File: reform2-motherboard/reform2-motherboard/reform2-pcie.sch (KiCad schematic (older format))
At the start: 31 parts, among them J10 1-2199230-6, J11 48099-5701, U11 679105700

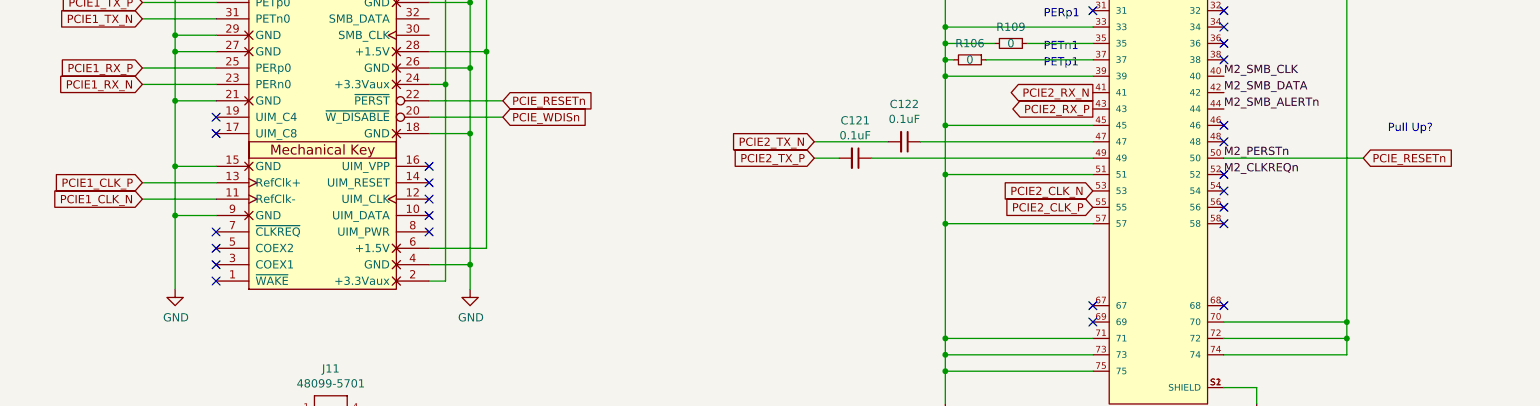
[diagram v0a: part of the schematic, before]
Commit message: WIP: reform 2 motherboard: tweaks for CL-SOM
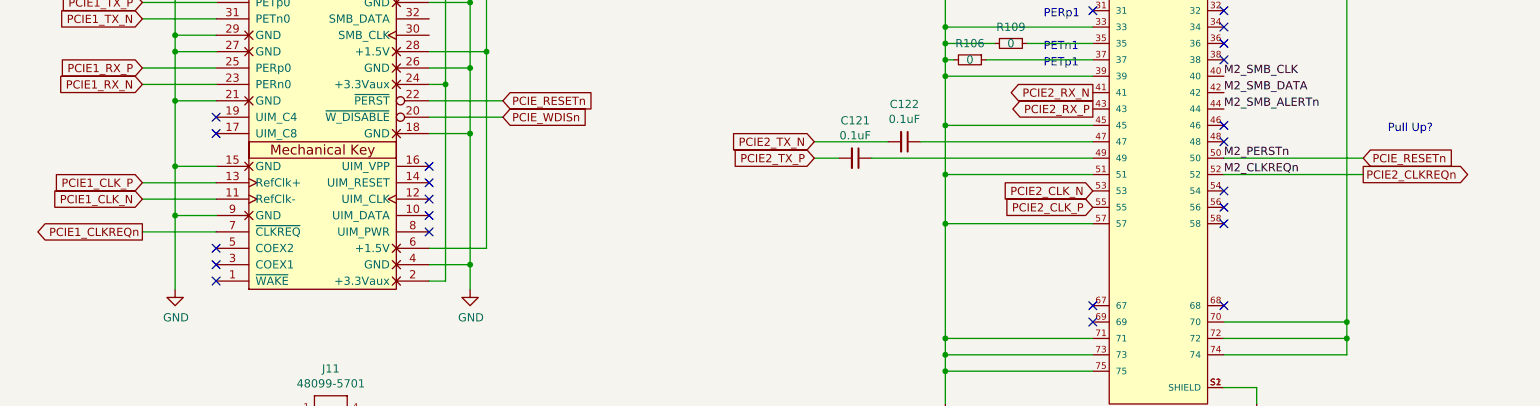
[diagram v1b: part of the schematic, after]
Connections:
- net labels added: PCIE1_CLKREQn, PCIE2_CLKREQn
- wire segments 175 -> 177
- no-connect marks 42 -> 40
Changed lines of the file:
@@
 Sheet 6 9
 Title "MNT Reform 2 PCIe"
-Date "2019-07-03"
-Rev "0.1"
+Date "2019-07-09"
+Rev "0.1.1"
 Comp "MNT Research GmbH"
 Comment1 "https://mntre.com"
@@
 NoConn ~ 2850 4500
 NoConn ~ 2850 4600
-NoConn ~ 2850 5200
 NoConn ~ 2850 5300
 NoConn ~ 2850 5400
@@
 NoConn ~ 4150 4900
 NoConn ~ 4150 4800
-NoConn ~ 9000 4850
 Text GLabel 4600 4500 2    50   Input ~ 0
 PCIE_WDISn
@@
 Wire Wire Line
 	4500 4100 4500 5300
+Text GLabel 2400 5200 0    50   Output ~ 0
+PCIE1_CLKREQn
+Wire Wire Line
+	2850 5200 2400 5200
+Text GLabel 9850 4850 2    50   Output ~ 0
+PCIE2_CLKREQn
+Wire Wire Line
+	9850 4850 9000 4850
 $EndSCHEMATC

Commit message: WIP: reform 2 motherboard: initial power section placement, routing tests
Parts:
- removed C56, C57, C62, C63: 220uF, Capacitor_SMD:CP_Elec_8x10, symbol Device:CP1_Small
- added C123, C124, C126, C83: 47uF, Capacitor_SMD:C_0603_1608Metric, symbol Device:C_Small
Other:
- note added: "TODO: symbol/connector pin mismatch"
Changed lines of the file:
@@
 Sheet 6 9
 Title "MNT Reform 2 PCIe"
-Date "2019-07-09"
-Rev "0.1.1"
+Date "2019-07-10"
+Rev "0.1.2"
 Comp "MNT Research GmbH"
 Comment1 "https://mntre.com"
@@
 	1    0    0    -1
 $EndComp
-$Comp
-L Device:CP1_Small C56
-U 1 1 60FCBB5A
-P 3600 2050
-F 0 "C56" H 3691 2096 50  0000 L CNN
-F 1 "220uF" H 3691 2005 50  0000 L CNN
-F 2 "Capacitor_SMD:CP_Elec_8x10" H 3600 2050 50  0001 C CNN
-F 3 "~" H 3600 2050 50  0001 C CNN
-F 4 "Panasonic" H 3600 2050 50  0001 C CNN "Manufacturer"
-F 5 "EEE-FT1H221GP" H 3600 2050 50  0001 C CNN "Manufacturer_No"
-	1    3600 2050
-	1    0    0    -1
-$EndComp
-$Comp
-L Device:CP1_Small C57
-U 1 1 60FCC62A
-P 4000 2050
-F 0 "C57" H 4091 2096 50  0000 L CNN
-F 1 "220uF" H 4091 2005 50  0000 L CNN
-F 2 "Capacitor_SMD:CP_Elec_8x10" H 4000 2050 50  0001 C CNN
-F 3 "~" H 4000 2050 50  0001 C CNN
-F 4 "Panasonic" H 4000 2050 50  0001 C CNN "Manufacturer"
-F 5 "EEE-FT1H221GP" H 4000 2050 50  0001 C CNN "Manufacturer_No"
-	1    4000 2050
-	1    0    0    -1
-$EndComp
 Wire Wire Line
 	1900 1950 2000 1950
@@
 	2800 1950 3200 1950
 Connection ~ 3200 1950
-Wire Wire Line
-	3200 1950 3600 1950
-Connection ~ 3600 1950
-Wire Wire Line
-	3600 1950 4000 1950
-Wire Wire Line
-	4000 2150 3600 2150
 Connection ~ 2400 2150
 Wire Wire Line
@@
 Wire Wire Line
 	3200 2150 2800 2150
-Connection ~ 3600 2150
-Wire Wire Line
-	3600 2150 3200 2150
 $Comp
 L power:GND #PWR0174
@@
 	1    0    0    -1
 $EndComp
-Connection ~ 4000 2150
 Text Notes 8200 1200 0    50   ~ 0
 1-2199230-5
@@
 	1    0    0    -1
 $EndComp
-$Comp
-L Device:CP1_Small C62
-U 1 1 61094295
-P 9000 1900
-F 0 "C62" H 9091 1946 50  0000 L CNN
-F 1 "220uF" H 9091 1855 50  0000 L CNN
-F 2 "Capacitor_SMD:CP_Elec_8x10" H 9000 1900 50  0001 C CNN
-F 3 "~" H 9000 1900 50  0001 C CNN
-F 4 "Panasonic" H 9000 1900 50  0001 C CNN "Manufacturer"
-F 5 "EEE-FT1H221GP" H 9000 1900 50  0001 C CNN "Manufacturer_No"
-	1    9000 1900
-	1    0    0    -1
-$EndComp
-$Comp
-L Device:CP1_Small C63
-U 1 1 6109429F
-P 9400 1900
-F 0 "C63" H 9491 1946 50  0000 L CNN
-F 1 "220uF" H 9491 1855 50  0000 L CNN
-F 2 "Capacitor_SMD:CP_Elec_8x10" H 9400 1900 50  0001 C CNN
-F 3 "~" H 9400 1900 50  0001 C CNN
-F 4 "Panasonic" H 9400 1900 50  0001 C CNN "Manufacturer"
-F 5 "EEE-FT1H221GP" H 9400 1900 50  0001 C CNN "Manufacturer_No"
-	1    9400 1900
-	1    0    0    -1
-$EndComp
 Connection ~ 7400 1800
 Wire Wire Line
@@
 	8200 1800 8600 1800
 Connection ~ 8600 1800
-Wire Wire Line
-	8600 1800 9000 1800
-Connection ~ 9000 1800
-Wire Wire Line
-	9000 1800 9400 1800
-Wire Wire Line
-	9400 2000 9000 2000
 Connection ~ 7800 2000
 Wire Wire Line
@@
 Wire Wire Line
 	8600 2000 8200 2000
-Connection ~ 9000 2000
-Wire Wire Line
-	9000 2000 8600 2000
 $Comp
 L power:GND #PWR0178
@@
 	1    0    0    -1
 $EndComp
-Connection ~ 9400 2000
 Wire Wire Line
 	7050 1800 7050 1750
 Wire Wire Line
 	7050 1800 7400 1800
-Wire Wire Line
-	9400 1800 9750 1800
-Connection ~ 9400 1800
 $Comp
 L reform2:48099-5701 J11
@@
 Wire Wire Line
 	9850 4850 9000 4850
+Wire Wire Line
+	3200 1950 3600 1950
+Wire Wire Line
+	3200 2150 3600 2150
+$Comp
+L Device:C_Small C83
+U 1 1 5EEACCAD
+P 3600 2050
+F 0 "C83" H 3692 2096 50  0000 L CNN
+F 1 "47uF" H 3692 2005 50  0000 L CNN
+F 2 "Capacitor_SMD:C_0603_1608Metric" H 3600 2050 50  0001 C CNN
+F 3 "~" H 3600 2050 50  0001 C CNN
+F 4 "Taiyo Yuden" H 3600 2050 50  0001 C CNN "Manufacturer"
+F 5 "LMK107BBJ106KALT" H 3600 2050 50  0001 C CNN "Manufacturer_No"
+	1    3600 2050
+	1    0    0    -1
+$EndComp
+Connection ~ 3600 1950
+Wire Wire Line
+	3600 1950 4000 1950
+Connection ~ 3600 2150
+Wire Wire Line
+	3600 2150 4000 2150
+$Comp
+L Device:C_Small C123
+U 1 1 5EEAD537
+P 4000 2050
+F 0 "C123" H 4092 2096 50  0000 L CNN
+F 1 "47uF" H 4092 2005 50  0000 L CNN
+F 2 "Capacitor_SMD:C_0603_1608Metric" H 4000 2050 50  0001 C CNN
+F 3 "~" H 4000 2050 50  0001 C CNN
+F 4 "Taiyo Yuden" H 4000 2050 50  0001 C CNN "Manufacturer"
+F 5 "LMK107BBJ106KALT" H 4000 2050 50  0001 C CNN "Manufacturer_No"
+	1    4000 2050
+	1    0    0    -1
+$EndComp
+Connection ~ 4000 2150
+Wire Wire Line
+	8600 2000 9000 2000
+Wire Wire Line
+	8600 1800 9000 1800
+$Comp
+L Device:C_Small C124
+U 1 1 5EEAEFE2
+P 9000 1900
+F 0 "C124" H 9092 1946 50  0000 L CNN
+F 1 "47uF" H 9092 1855 50  0000 L CNN
+F 2 "Capacitor_SMD:C_0603_1608Metric" H 9000 1900 50  0001 C CNN
+F 3 "~" H 9000 1900 50  0001 C CNN
+F 4 "TDK" H 9000 1900 50  0001 C CNN "Manufacturer"
+F 5 "CGA3E2X8R1E104K080AE" H 9000 1900 50  0001 C CNN "Manufacturer_No"
+	1    9000 1900
+	1    0    0    -1
+$EndComp
+Connection ~ 9000 1800
+Wire Wire Line
+	9000 1800 9400 1800
+Connection ~ 9000 2000
+Wire Wire Line
+	9000 2000 9400 2000
+$Comp
+L Device:C_Small C126
+U 1 1 5EEAF1A5
+P 9400 1900
+F 0 "C126" H 9492 1946 50  0000 L CNN
+F 1 "47uF" H 9492 1855 50  0000 L CNN
+F 2 "Capacitor_SMD:C_0603_1608Metric" H 9400 1900 50  0001 C CNN
+F 3 "~" H 9400 1900 50  0001 C CNN
+F 4 "TDK" H 9400 1900 50  0001 C CNN "Manufacturer"
+F 5 "CGA3E2X8R1E104K080AE" H 9400 1900 50  0001 C CNN "Manufacturer_No"
+	1    9400 1900
+	1    0    0    -1
+$EndComp
+Connection ~ 9400 1800
+Wire Wire Line
+	9400 1800 9750 1800
+Connection ~ 9400 2000
+Text Notes 6600 2300 0    50   ~ 0
+TODO: symbol/connector pin mismatch
 $EndSCHEMATC

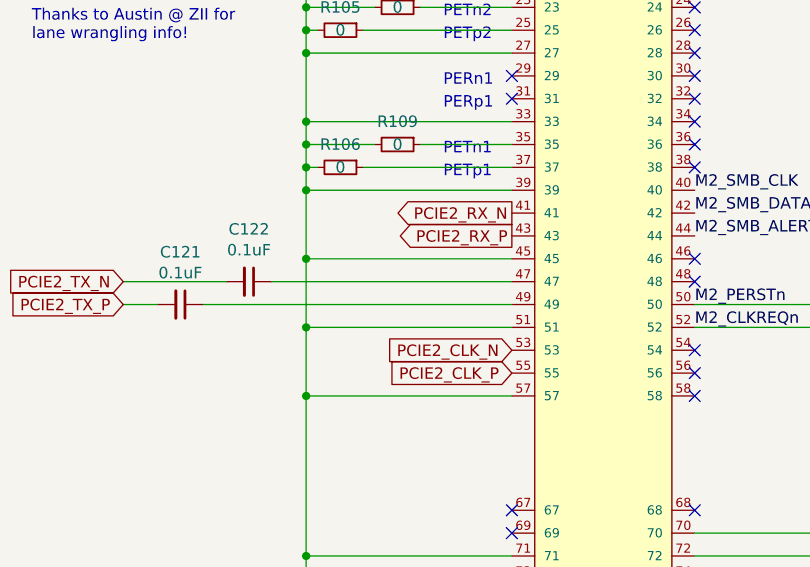
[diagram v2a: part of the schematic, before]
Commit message: WIP: reform2 motherboard routing: NVMe and some DSI/eDP
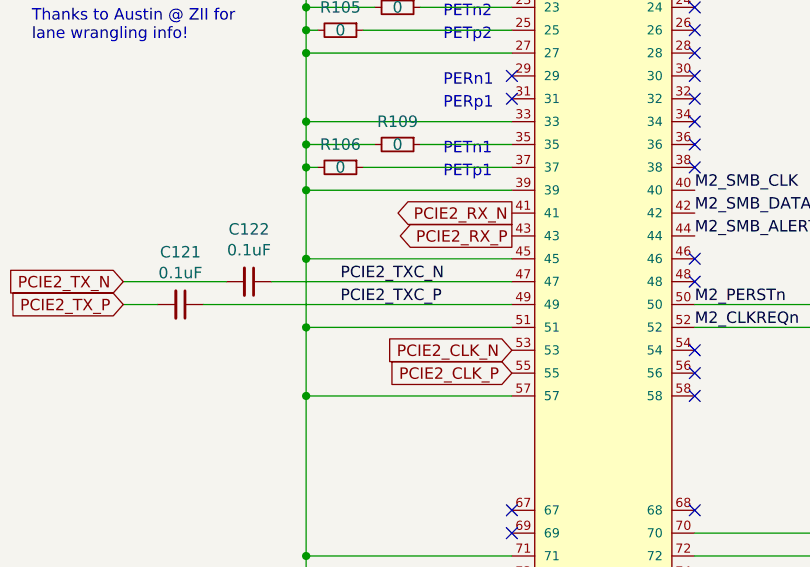
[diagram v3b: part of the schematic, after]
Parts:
- J10: footprint footprints:TE_1-2199230-5 -> footprints:TE_1-2199230-6
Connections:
- net PCIE2_TXC_N: now reaches C122.1, J10.47
- net PCIE2_TXC_P: now reaches C121.1, J10.49
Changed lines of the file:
@@
 F 0 "J10" H 8600 2100 50  0000 C CNN
 F 1 "1-2199230-6" H 8600 2200 50  0000 C CNN
-F 2 "footprints:TE_1-2199230-5" H 8600 4250 50  0001 L BNN
+F 2 "footprints:TE_1-2199230-6" H 8600 4250 50  0001 L BNN
 F 3 "" H 8600 4250 50  0001 L BNN
 F 4 "TE Connectivity" H 8600 4250 50  0001 L BNN "Field4"
@@
 Text Notes 6600 2300 0    50   ~ 0
 TODO: symbol/connector pin mismatch
+Text Label 7450 4650 0    50   ~ 0
+PCIE2_TXC_N
+Text Label 7450 4750 0    50   ~ 0
+PCIE2_TXC_P
 $EndSCHEMATC

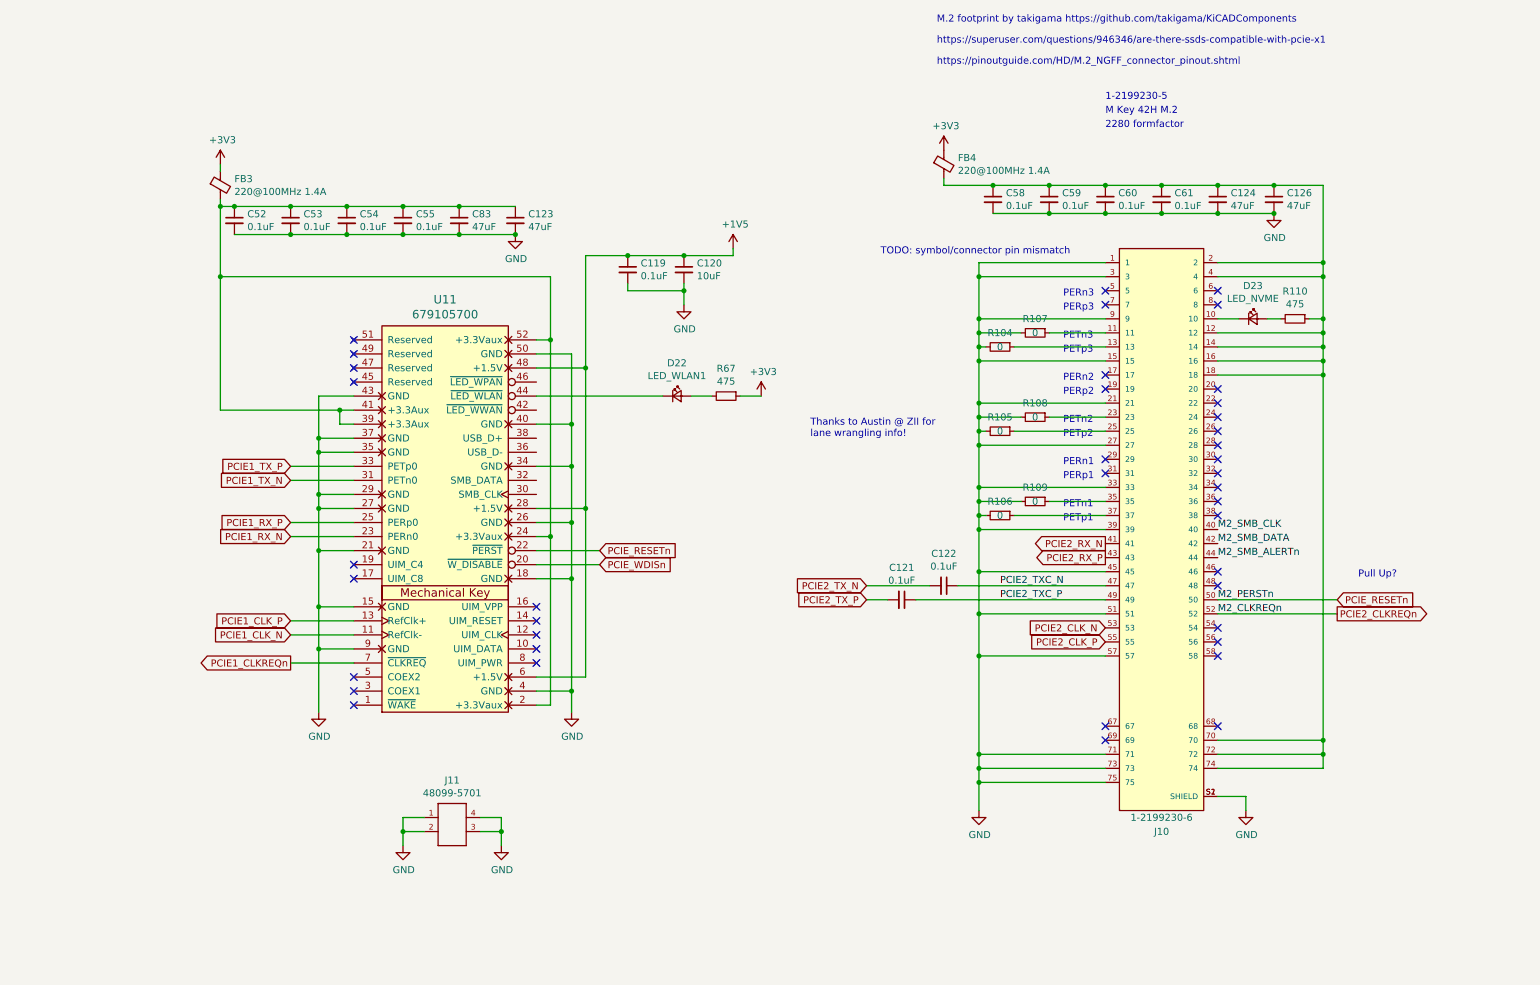
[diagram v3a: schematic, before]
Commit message: reform2 motherboard: pinout and footprint checks completed; ERC checks fixed 100%
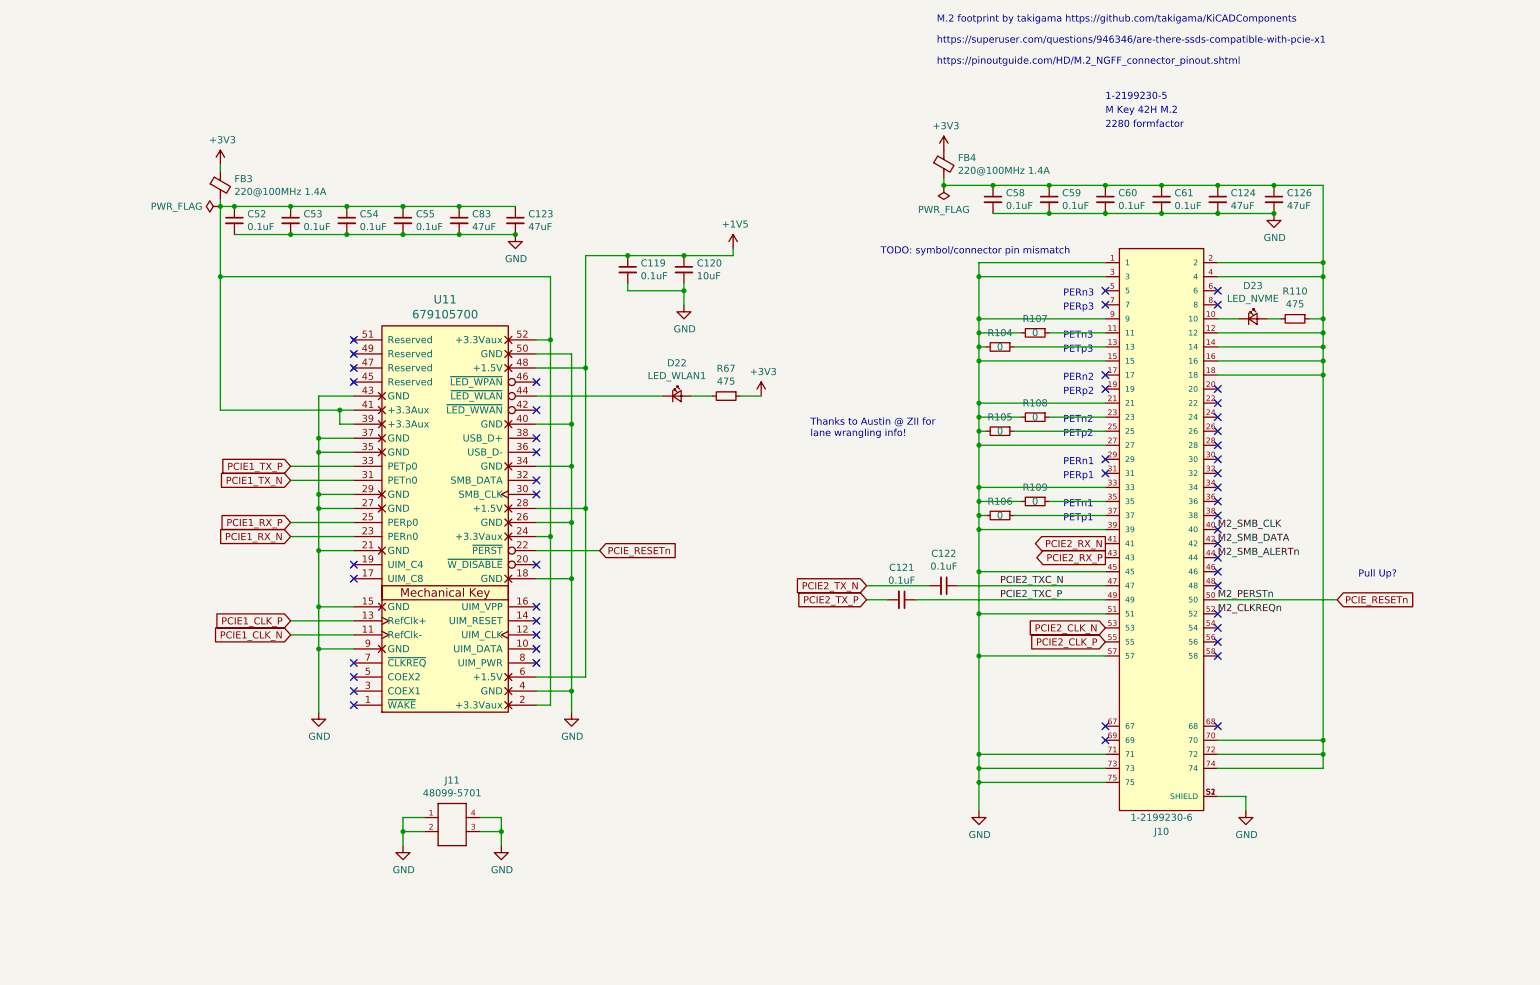
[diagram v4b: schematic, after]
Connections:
- net PCIE1_CLKREQn: no longer names the net of U11.7 (~CLKREQ)
- net PCIE2_CLKREQn renamed M2_CLKREQn
- net PCIE_WDISn: no longer names the net of U11.20 (~W_DISABLE)
- no-connect marks 40 -> 52
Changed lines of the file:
@@
 Wire Wire Line
 	9000 3150 9750 3150
-Connection ~ 9750 3150
 $Comp
 L Device:LED_Small D23
@@
 Wire Wire Line
 	9850 4750 9000 4750
-Text Label 9000 4350 0    50   ~ 0
-M2_SMB_DATA
-Text Label 9000 4250 0    50   ~ 0
-M2_SMB_CLK
-Text Label 9000 4450 0    50   ~ 0
-M2_SMB_ALERTn
 NoConn ~ 9000 4550
 NoConn ~ 9000 4650
@@
 	9750 5950 9000 5950
 Wire Wire Line
-	9750 3150 9750 5750
-Wire Wire Line
 	9000 5850 9750 5850
 Connection ~ 9750 5850
@@
 Wire Wire Line
 	9750 5750 9000 5750
-Connection ~ 9750 5750
 Wire Wire Line
 	9750 5750 9750 5850
@@
 NoConn ~ 4150 4900
 NoConn ~ 4150 4800
-Text GLabel 4600 4500 2    50   Input ~ 0
-PCIE_WDISn
-Wire Wire Line
-	4600 4500 4150 4500
 $Comp
 L Device:C_Small C120
@@
 Wire Wire Line
 	4500 4100 4500 5300
-Text GLabel 2400 5200 0    50   Output ~ 0
-PCIE1_CLKREQn
-Wire Wire Line
-	2850 5200 2400 5200
-Text GLabel 9850 4850 2    50   Output ~ 0
-PCIE2_CLKREQn
-Wire Wire Line
-	9850 4850 9000 4850
 Wire Wire Line
 	3200 1950 3600 1950
@@
 Text Label 7450 4750 0    50   ~ 0
 PCIE2_TXC_P
+NoConn ~ 2850 5200
+NoConn ~ 9000 4850
+NoConn ~ 4150 3200
+NoConn ~ 4150 3400
+NoConn ~ 4150 3600
+NoConn ~ 4150 3700
+NoConn ~ 4150 3900
+NoConn ~ 4150 4000
+NoConn ~ 4150 4500
+Connection ~ 9750 5750
+Connection ~ 9750 3150
+Wire Wire Line
+	9750 3150 9750 5750
+Text Label 9000 4450 0    50   ~ 0
+M2_SMB_ALERTn
+Text Label 9000 4250 0    50   ~ 0
+M2_SMB_CLK
+Text Label 9000 4350 0    50   ~ 0
+M2_SMB_DATA
+NoConn ~ 9000 4250
+NoConn ~ 9000 4350
+NoConn ~ 9000 4450
+$Comp
+L power:PWR_FLAG #FLG0107
+U 1 1 64915E59
+P 1900 1950
+F 0 "#FLG0107" H 1900 2025 50  0001 C CNN
+F 1 "PWR_FLAG" V 1900 2077 50  0000 L CNN
+F 2 "" H 1900 1950 50  0001 C CNN
+F 3 "~" H 1900 1950 50  0001 C CNN
+	1    1900 1950
+	0    -1   -1   0
+$EndComp
+$Comp
+L power:PWR_FLAG #FLG0108
+U 1 1 6491670E
+P 7050 1800
+F 0 "#FLG0108" H 7050 1875 50  0001 C CNN
+F 1 "PWR_FLAG" H 7050 1973 50  0000 C CNN
+F 2 "" H 7050 1800 50  0001 C CNN
+F 3 "~" H 7050 1800 50  0001 C CNN
+	1    7050 1800
+	-1   0    0    1
+$EndComp
+Connection ~ 7050 1800
 $EndSCHEMATC
